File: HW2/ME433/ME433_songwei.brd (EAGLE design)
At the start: 50 x 50 mm, 22 parts, among them J1 USB-MB-H

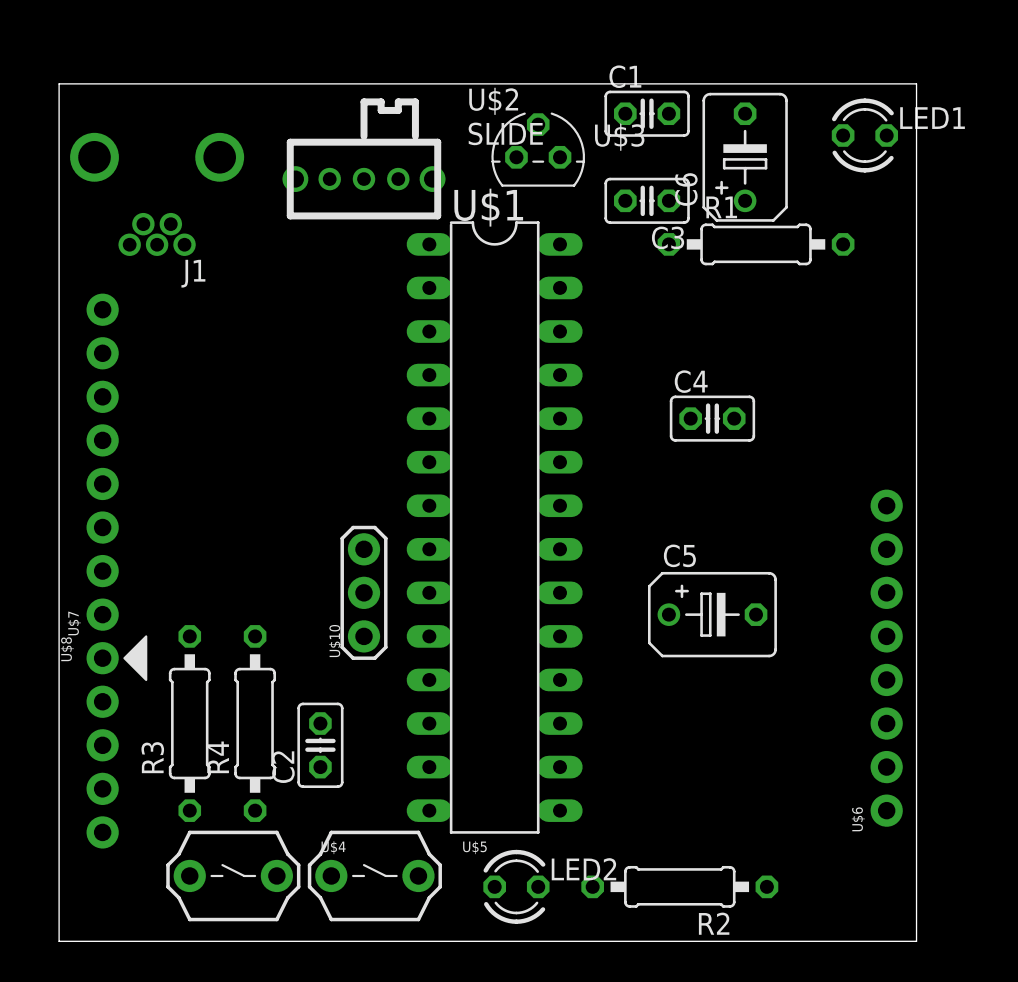
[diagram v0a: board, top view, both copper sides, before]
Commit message: Updated .brd file, connections done
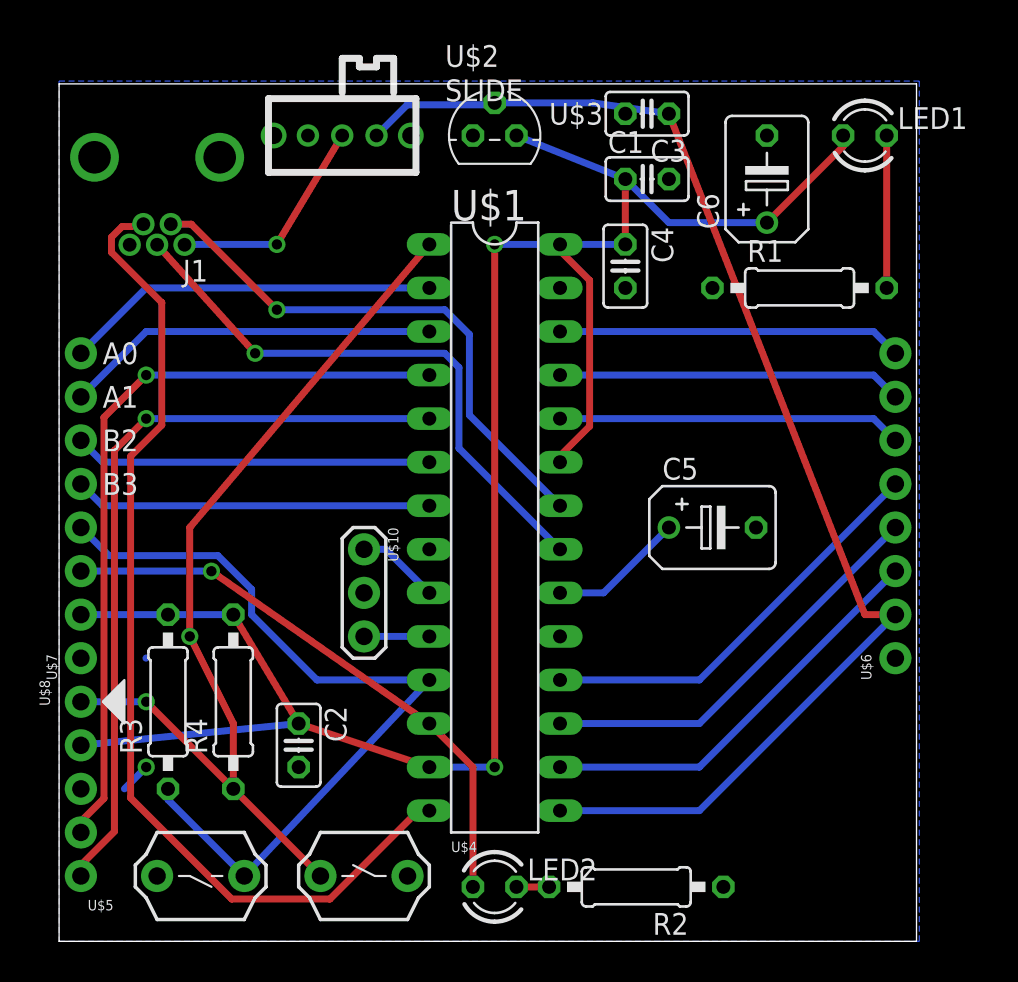
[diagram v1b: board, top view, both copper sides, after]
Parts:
- moved C4 10.2 mm to (33.0, 39.4), turned to 270 degrees
- moved U$5 10.2 mm to (8.26, 3.81), turned to 180 degrees
- moved U$6 8.90 mm to (48.8, 16.5)
- moved U$4 7.62 mm to (17.8, 3.81)
- moved C3 5.08 mm to (34.3, 48.3)
- moved C5 5.08 mm to (38.1, 24.1)
- moved C1 3.81 mm to (34.3, 44.5)
- moved R1 3.59 mm to (43.2, 38.1)
- moved U$3 2.84 mm to (25.4, 47.0)
- moved U$8 2.84 mm to (1.27, 14.0)
- moved U$2 2.84 mm to (16.5, 47.0)
- moved U$7 2.84 mm to (1.27, 16.5)
- moved R2 2.54 mm to (33.7, 3.17)
- moved R3 1.80 mm to (6.35, 14.0)
- moved R4 1.80 mm to (10.2, 14.0)
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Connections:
- removed net 3V3: U$1.23
- net +3V3: now also U$1.23
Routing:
- net +3V3: track 0.00 -> 120.4 mm, vias 0 -> 2
- net +5V: track 0.00 -> 75.3 mm
- net USBID: track 0.00 -> 58.8 mm
- net MCLR: track 0.00 -> 55.6 mm, vias 0 -> 2
- net B4/USER: track 0.00 -> 47.5 mm
- net PGD: track 0.00 -> 44.8 mm, vias 0 -> 1
- net PGC: track 0.00 -> 44.8 mm, vias 0 -> 1
- net D+: track 0.00 -> 33.8 mm, vias 0 -> 1
- net A4/LED: track 0.00 -> 33.7 mm, vias 0 -> 1
- net D-: track 0.00 -> 32.3 mm, vias 0 -> 1
- net B9: track 0.00 -> 24.3 mm
- net B8: track 0.00 -> 24.3 mm
- net B7: track 0.00 -> 24.3 mm
- net A1: track 0.00 -> 21.9 mm
- net A0: track 0.00 -> 21.9 mm
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- added copper zone on layer 16, net GND
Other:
- board text added: "A0"
- board text added: "A1"
- board text added: "B2"
- board text added: "B3"

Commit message: Updated all silkscreen on .brd
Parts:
- moved C5 3.59 mm to (35.6, 26.7)
- moved C3 1.27 mm to (34.3, 47.0)
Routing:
- net +5V: track 75.3 -> 74.4 mm
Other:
- board text added: "+3V3"
- board text added: "+5V"
- board text added: "A4/USER"
- board text added: "B13"
- board text added: "B14"
- board text added: "B15"
- board text added: "B4/USER"
- board text added: "B7"
- board text added: "B8"
- board text added: "B9"
- board text added: "D+"
- board text added: "D-"
- board text added: "GND"
- board text added: "USBID"
- board text added: "VBUS"
